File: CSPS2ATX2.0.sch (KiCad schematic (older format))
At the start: 63 parts, among them J1 Conn_02x32_Counter_Clockwise, J10 IDE/SATA, J101 USB_C_Receptacle_USB2.0, J102 Conn_02x03_Odd_Even, J103 Conn_01x04, J104 Conn_01x04, J2 GW_24p_ATX, J3 GW_PCIe/CPU, J4 GW_PCIe/CPU, J5 GW_PCIe/CPU, J6 GW_PCIe/CPU, J7 GW_PCIe/CPU, J8 GW_PCIe/CPU, J9 IDE/SATA, SW101 SW_Push, U1 TPS3511, U101 ATmega328P-AU, U102 CH340C, U2 PW22ASAB, U3 PW22ASAB, U4 Mini360, Y101 16MHz

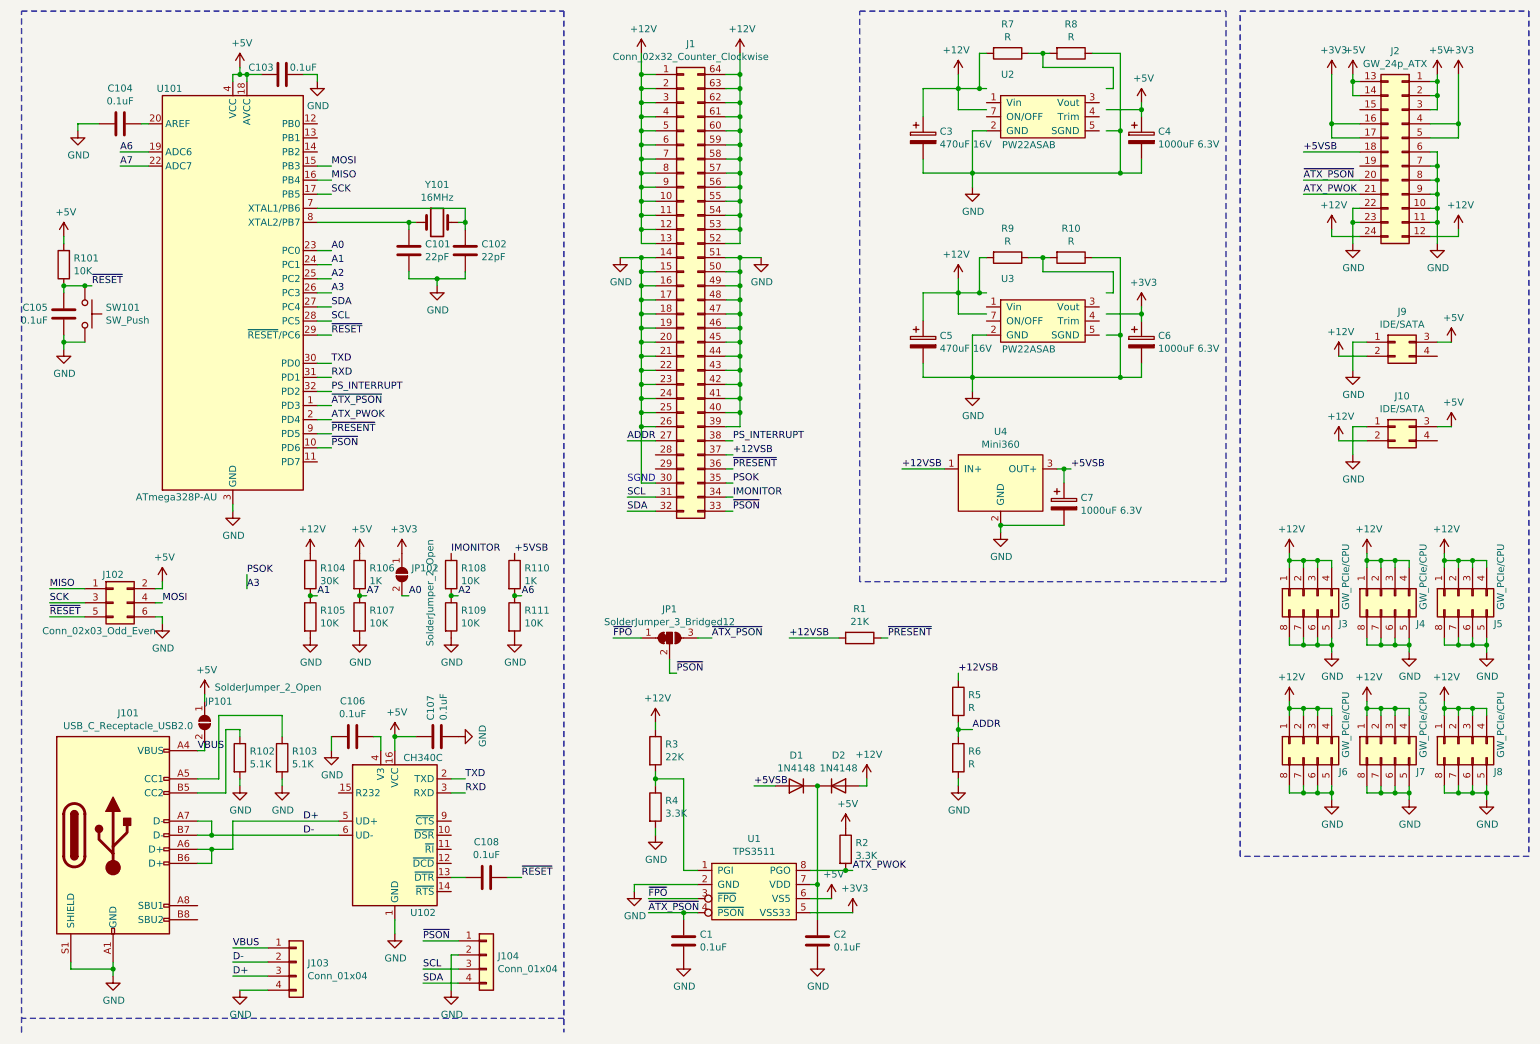
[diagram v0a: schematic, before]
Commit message: confirm trim resistor
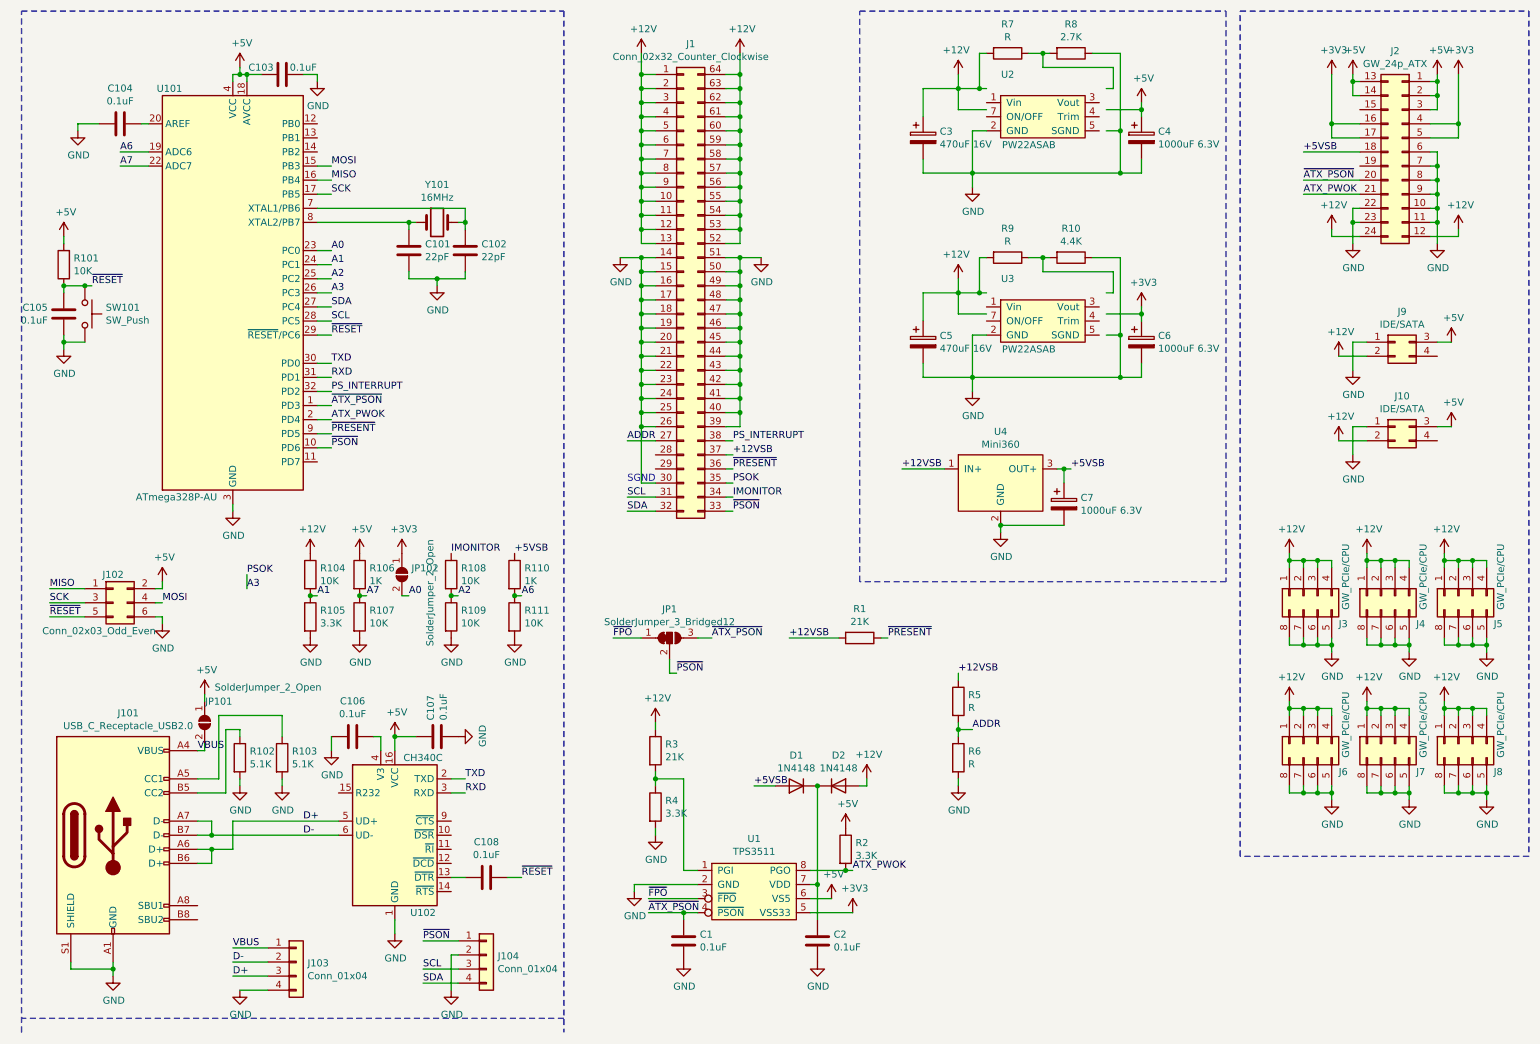
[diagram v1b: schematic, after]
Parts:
- R10: value R -> 4.4K
- R104: value 30K -> 10K
- R105: value 10K -> 3.3K
- R3: value 22K -> 21K
- R8: value R -> 2.7K
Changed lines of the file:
@@
 P 5000 5750
 F 0 "R3" H 5070 5796 50  0000 L CNN
-F 1 "22K" H 5070 5705 50  0000 L CNN
+F 1 "21K" H 5070 5705 50  0000 L CNN
 F 2 "Resistor_SMD:R_0805_2012Metric" V 4930 5750 50  0001 C CNN
 F 3 "~" H 5000 5750 50  0001 C CNN
@@
 P 2550 4800
 F 0 "R105" H 2620 4846 50  0000 L CNN
-F 1 "10K" H 2620 4755 50  0000 L CNN
+F 1 "3.3K" H 2620 4755 50  0000 L CNN
 F 2 "Resistor_SMD:R_0805_2012Metric" V 2480 4800 50  0001 C CNN
 F 3 "~" H 2550 4800 50  0001 C CNN
@@
 P 2550 4500
 F 0 "R104" H 2620 4546 50  0000 L CNN
-F 1 "30K" H 2620 4455 50  0000 L CNN
+F 1 "10K" H 2620 4455 50  0000 L CNN
 F 2 "Resistor_SMD:R_0805_2012Metric" V 2480 4500 50  0001 C CNN
 F 3 "~" H 2550 4500 50  0001 C CNN
@@
 P 7950 800
 F 0 "R8" V 7743 800 50  0000 C CNN
-F 1 "R" V 7834 800 50  0000 C CNN
+F 1 "2.7K" V 7834 800 50  0000 C CNN
 F 2 "Resistor_SMD:R_0805_2012Metric" V 7880 800 50  0001 C CNN
 F 3 "~" H 7950 800 50  0001 C CNN
@@
 P 7950 2250
 F 0 "R10" V 7743 2250 50  0000 C CNN
-F 1 "R" V 7834 2250 50  0000 C CNN
+F 1 "4.4K" V 7834 2250 50  0000 C CNN
 F 2 "Resistor_SMD:R_0805_2012Metric" V 7880 2250 50  0001 C CNN
 F 3 "~" H 7950 2250 50  0001 C CNN

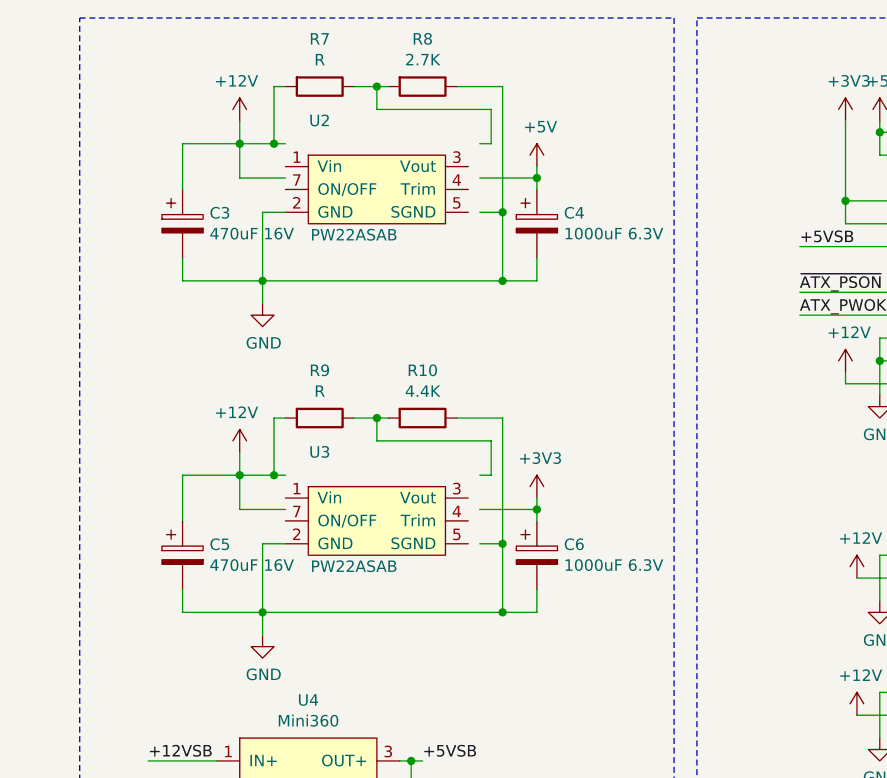
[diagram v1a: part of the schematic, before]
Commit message: remove R7 R9
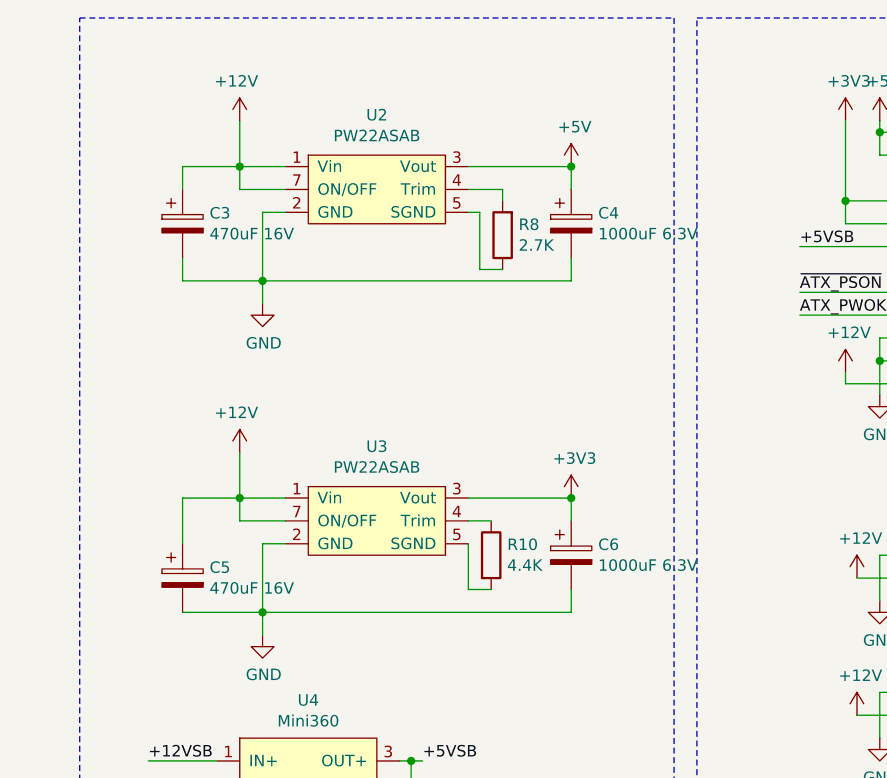
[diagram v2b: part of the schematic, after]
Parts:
- removed R7, R9: R, Resistor_SMD:R_0805_2012Metric, symbol Device:R
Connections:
- net +12V: now also U2.1 (Vin), U2.7 (ON/OFF), U3.1 (Vin), U3.7 (ON/OFF)
- net +3V3: now also U3.3 (Vout)
- net +5V: now also U2.3 (Vout)
- net GND: no longer R10.1, R8.1
- net at U2.4 (Trim): now also R8.2
- net at U2.5 (SGND): now also R8.1
- net at R10.2: now also U3.5 (SGND)
- net at U3.4 (Trim): now also R10.1
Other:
- moved on the sheet: C4, C5, C6, R10, R8
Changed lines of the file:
@@
 $EndComp
 Wire Wire Line
-	7150 950  7150 1050
-Connection ~ 7150 1050
+	7150 950  7150 1150
+Connection ~ 7150 1150
 $Comp
 L Device:CP C3
@@
 L Device:CP C4
 U 1 1 607CC1CF
-P 8450 1400
-F 0 "C4" H 8568 1446 50  0000 L CNN
-F 1 "1000uF 6.3V" H 8568 1355 50  0000 L CNN
-F 2 "Capacitor_SMD:CP_Elec_8x10" H 8488 1250 50  0001 C CNN
-F 3 "~" H 8450 1400 50  0001 C CNN
-	1    8450 1400
+P 8600 1400
+F 0 "C4" H 8718 1446 50  0000 L CNN
+F 1 "1000uF 6.3V" H 8718 1355 50  0000 L CNN
+F 2 "Capacitor_SMD:CP_Elec_8x10" H 8638 1250 50  0001 C CNN
+F 3 "~" H 8600 1400 50  0001 C CNN
+	1    8600 1400
 	1    0    0    -1
 $EndComp
@@
 Connection ~ 7250 1650
 Wire Wire Line
-	6900 1050 7150 1050
-Wire Wire Line
-	7150 1200 7150 1050
+	6900 1150 7150 1150
+Wire Wire Line
+	7150 1250 7150 1150
 Wire Wire Line
 	7250 1350 7250 1650
 Wire Wire Line
-	8450 1650 8450 1550
+	8600 1650 8600 1550
 Wire Wire Line
 	6900 1650 7250 1650
@@
 	6900 1550 6900 1650
 Wire Wire Line
-	6900 1050 6900 1250
-Wire Wire Line
-	8200 1200 8450 1200
-Wire Wire Line
-	8450 1200 8450 1250
-$Comp
-L Device:R R7
-U 1 1 609ABD58
-P 7500 800
-F 0 "R7" V 7293 800 50  0000 C CNN
-F 1 "R" V 7384 800 50  0000 C CNN
-F 2 "Resistor_SMD:R_0805_2012Metric" V 7430 800 50  0001 C CNN
-F 3 "~" H 7500 800 50  0001 C CNN
-	1    7500 800
-	0    1    1    0
-$EndComp
+	6900 1150 6900 1250
+Wire Wire Line
+	8150 1150 8600 1150
+Wire Wire Line
+	8600 1150 8600 1250
 $Comp
 L Device:R R8
 U 1 1 609AD201
-P 7950 800
-F 0 "R8" V 7743 800 50  0000 C CNN
-F 1 "2.7K" V 7834 800 50  0000 C CNN
-F 2 "Resistor_SMD:R_0805_2012Metric" V 7880 800 50  0001 C CNN
-F 3 "~" H 7950 800 50  0001 C CNN
-	1    7950 800
-	0    1    1    0
+P 8300 1450
+F 0 "R8" H 8230 1404 50  0000 R CNN
+F 1 "2.7K" H 8230 1495 50  0000 R CNN
+F 2 "Resistor_SMD:R_0805_2012Metric" V 8230 1450 50  0001 C CNN
+F 3 "~" H 8300 1450 50  0001 C CNN
+	1    8300 1450
+	-1   0    0    1
 $EndComp
 Wire Wire Line
 	7350 1350 7250 1350
 Wire Wire Line
-	7350 1200 7150 1200
-Wire Wire Line
-	7150 1050 7300 1050
+	7350 1250 7150 1250
 $Comp
 L KCORES_Converter_DCDC:PW22ASAB U2
 U 1 1 60724679
 P 7450 1400
-F 0 "U2" H 7500 1850 50  0000 C CNN
-F 1 "PW22ASAB" H 7650 1350 50  0000 C CNN
+F 0 "U2" H 7750 1875 50  0000 C CNN
+F 1 "PW22ASAB" H 7750 1784 50  0000 C CNN
 F 2 "KCORES_Converter_DCDC:PW22ASAB" H 7450 1700 50  0001 C CNN
 F 3 "" H 7450 1700 50  0001 C CNN
@@
 	1    0    0    -1
 $EndComp
-Wire Wire Line
-	8200 1050 8250 1050
-Wire Wire Line
-	8250 1050 8250 900
-Wire Wire Line
-	8250 900  7750 900
-Wire Wire Line
-	7750 900  7750 800
-Wire Wire Line
-	7750 800  7800 800
-Wire Wire Line
-	7250 1650 8300 1650
-Wire Wire Line
-	8100 800  8300 800
-Wire Wire Line
-	8300 800  8300 1350
-Connection ~ 8300 1650
-Wire Wire Line
-	8300 1650 8450 1650
-Wire Wire Line
-	8200 1350 8300 1350
-Connection ~ 8300 1350
-Wire Wire Line
-	8300 1350 8300 1650
-Wire Wire Line
-	7650 800  7750 800
-Connection ~ 7750 800
-Wire Wire Line
-	7350 800  7300 800
-Wire Wire Line
-	7300 800  7300 1050
-Connection ~ 7300 1050
-Wire Wire Line
-	7300 1050 7350 1050
 $Comp
 L power:+5V #PWR0113
 U 1 1 60A83744
-P 8450 1150
-F 0 "#PWR0113" H 8450 1000 50  0001 C CNN
-F 1 "+5V" H 8465 1323 50  0000 C CNN
-F 2 "" H 8450 1150 50  0001 C CNN
-F 3 "" H 8450 1150 50  0001 C CNN
-	1    8450 1150
-	1    0    0    -1
-$EndComp
-Wire Wire Line
-	8450 1200 8450 1150
-Connection ~ 8450 1200
+P 8600 1150
+F 0 "#PWR0113" H 8600 1000 50  0001 C CNN
+F 1 "+5V" H 8615 1323 50  0000 C CNN
+F 2 "" H 8600 1150 50  0001 C CNN
+F 3 "" H 8600 1150 50  0001 C CNN
+	1    8600 1150
+	1    0    0    -1
+$EndComp
+Connection ~ 8600 1150
 $Comp
 L power:+12V #PWR0114
@@
 $EndComp
 Wire Wire Line
-	7150 2400 7150 2500
-Connection ~ 7150 2500
+	7150 2400 7150 2600
+Connection ~ 7150 2600
 $Comp
 L Device:CP C5
 U 1 1 60DCFB2B
-P 6900 2850
-F 0 "C5" H 7018 2896 50  0000 L CNN
-F 1 "470uF 16V" H 7018 2805 50  0000 L CNN
-F 2 "Capacitor_SMD:CP_Elec_8x10" H 6938 2700 50  0001 C CNN
-F 3 "~" H 6900 2850 50  0001 C CNN
-	1    6900 2850
+P 6900 2950
+F 0 "C5" H 7018 2996 50  0000 L CNN
+F 1 "470uF 16V" H 7018 2905 50  0000 L CNN
+F 2 "Capacitor_SMD:CP_Elec_8x10" H 6938 2800 50  0001 C CNN
+F 3 "~" H 6900 2950 50  0001 C CNN
+	1    6900 2950
 	1    0    0    -1
 $EndComp
@@
 L Device:CP C6
 U 1 1 60DCFB31
-P 8450 2850
-F 0 "C6" H 8568 2896 50  0000 L CNN
-F 1 "1000uF 6.3V" H 8568 2805 50  0000 L CNN
-F 2 "Capacitor_SMD:CP_Elec_8x10" H 8488 2700 50  0001 C CNN
-F 3 "~" H 8450 2850 50  0001 C CNN
-	1    8450 2850
+P 8600 2850
+F 0 "C6" H 8718 2896 50  0000 L CNN
+F 1 "1000uF 6.3V" H 8718 2805 50  0000 L CNN
+F 2 "Capacitor_SMD:CP_Elec_8x10" H 8638 2700 50  0001 C CNN
+F 3 "~" H 8600 2850 50  0001 C CNN
+	1    8600 2850
 	1    0    0    -1
 $EndComp
@@
 Connection ~ 7250 3100
 Wire Wire Line
-	6900 2500 7150 2500
-Wire Wire Line
-	7150 2650 7150 2500
+	6900 2600 7150 2600
+Wire Wire Line
+	7150 2700 7150 2600
 Wire Wire Line
 	7250 2800 7250 3100
 Wire Wire Line
-	8450 3100 8450 3000
+	8600 3100 8600 3000
 Wire Wire Line
 	6900 3100 7250 3100
 Wire Wire Line
-	6900 3000 6900 3100
-Wire Wire Line
-	6900 2500 6900 2700
-Wire Wire Line
-	8200 2650 8450 2650
-Wire Wire Line
-	8450 2650 8450 2700
-$Comp
-L Device:R R9
-U 1 1 60DCFB48
-P 7500 2250
-F 0 "R9" V 7293 2250 50  0000 C CNN
-F 1 "R" V 7384 2250 50  0000 C CNN
-F 2 "Resistor_SMD:R_0805_2012Metric" V 7430 2250 50  0001 C CNN
-F 3 "~" H 7500 2250 50  0001 C CNN
-	1    7500 2250
-	0    1    1    0
-$EndComp
-$Comp
-L Device:R R10
-U 1 1 60DCFB4E
-P 7950 2250
-F 0 "R10" V 7743 2250 50  0000 C CNN
-F 1 "4.4K" V 7834 2250 50  0000 C CNN
-F 2 "Resistor_SMD:R_0805_2012Metric" V 7880 2250 50  0001 C CNN
-F 3 "~" H 7950 2250 50  0001 C CNN
-	1    7950 2250
-	0    1    1    0
-$EndComp
+	6900 2600 6900 2800
+Wire Wire Line
+	8150 2600 8600 2600
+Wire Wire Line
+	8600 2600 8600 2700
 Wire Wire Line
 	7350 2800 7250 2800
 Wire Wire Line
-	7350 2650 7150 2650
-Wire Wire Line
-	7150 2500 7300 2500
-$Comp
-L KCORES_Converter_DCDC:PW22ASAB U3
-U 1 1 60DCFB57
-P 7450 2850
-F 0 "U3" H 7500 3300 50  0000 C CNN
-F 1 "PW22ASAB" H 7650 2800 50  0000 C CNN
-F 2 "KCORES_Converter_DCDC:PW22ASAB" H 7450 3150 50  0001 C CNN
-F 3 "" H 7450 3150 50  0001 C CNN
-	1    7450 2850
-	1    0    0    -1
-$EndComp
-Wire Wire Line
-	8200 2500 8250 2500
-Wire Wire Line
-	8250 2500 8250 2350
-Wire Wire Line
-	8250 2350 7750 2350
-Wire Wire Line
-	7750 2350 7750 2250
-Wire Wire Line
-	7750 2250 7800 2250
-Wire Wire Line
-	7250 3100 8300 3100
-Wire Wire Line
-	8100 2250 8300 2250
-Wire Wire Line
-	8300 2250 8300 2800
-Connection ~ 8300 3100
-Wire Wire Line
-	8300 3100 8450 3100
-Wire Wire Line
-	8200 2800 8300 2800
-Connection ~ 8300 2800
-Wire Wire Line
-	8300 2800 8300 3100
-Wire Wire Line
-	7650 2250 7750 2250
-Connection ~ 7750 2250
-Wire Wire Line
-	7350 2250 7300 2250
-Wire Wire Line
-	7300 2250 7300 2500
-Connection ~ 7300 2500
-Wire Wire Line
-	7300 2500 7350 2500
-Wire Wire Line
-	8450 2650 8450 2600
-Connection ~ 8450 2650
+	7350 2700 7150 2700
+Connection ~ 8600 2600
 $Comp
 L power:+3V3 #PWR0127
 U 1 1 60F0D764
-P 8450 2600
-F 0 "#PWR0127" H 8450 2450 50  0001 C CNN
-F 1 "+3V3" H 8465 2773 50  0000 C CNN
-F 2 "" H 8450 2600 50  0001 C CNN
-F 3 "" H 8450 2600 50  0001 C CNN
-	1    8450 2600
+P 8600 2600
+F 0 "#PWR0127" H 8600 2450 50  0001 C CNN
+F 1 "+3V3" H 8615 2773 50  0000 C CNN
+F 2 "" H 8600 2600 50  0001 C CNN
+F 3 "" H 8600 2600 50  0001 C CNN
+	1    8600 2600
 	1    0    0    -1
 $EndComp
@@
 	0    1    1    0
 $EndComp
+Wire Wire Line
+	7250 1650 8600 1650
+Wire Wire Line
+	7250 3100 8600 3100
+Wire Wire Line
+	7150 2600 7350 2600
+Wire Wire Line
+	7150 1150 7350 1150
+Wire Wire Line
+	8150 1250 8300 1250
+Wire Wire Line
+	8300 1250 8300 1300
+Wire Wire Line
+	8200 1350 8200 1600
+Wire Wire Line
+	8200 1600 8300 1600
+Wire Wire Line
+	8150 1350 8200 1350
+$Comp
+L Device:R R10
+U 1 1 60DCFB4E
+P 8250 2850
+F 0 "R10" H 8320 2896 50  0000 L CNN
+F 1 "4.4K" H 8320 2805 50  0000 L CNN
+F 2 "Resistor_SMD:R_0805_2012Metric" V 8180 2850 50  0001 C CNN
+F 3 "~" H 8250 2850 50  0001 C CNN
+	1    8250 2850
+	1    0    0    -1
+$EndComp
+$Comp
+L KCORES_Converter_DCDC:PW22ASAB U3
+U 1 1 60DCFB57
+P 7450 2850
+F 0 "U3" H 7750 3325 50  0000 C CNN
+F 1 "PW22ASAB" H 7750 3234 50  0000 C CNN
+F 2 "KCORES_Converter_DCDC:PW22ASAB" H 7450 3150 50  0001 C CNN
+F 3 "" H 7450 3150 50  0001 C CNN
+	1    7450 2850
+	1    0    0    -1
+$EndComp
+Wire Wire Line
+	8150 2700 8250 2700
+Wire Wire Line
+	8150 2800 8150 3000
+Wire Wire Line
+	8150 3000 8250 3000
 $EndSCHEMATC
